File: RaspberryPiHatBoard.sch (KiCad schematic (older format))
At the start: 49 parts

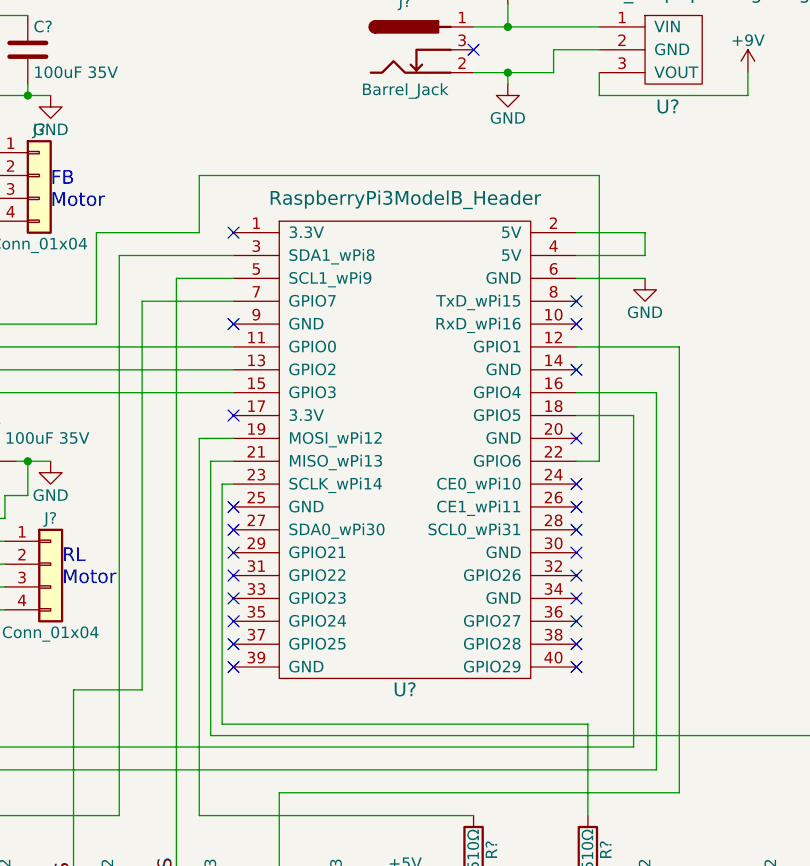
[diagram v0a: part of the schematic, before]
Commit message: Converted to pigpio
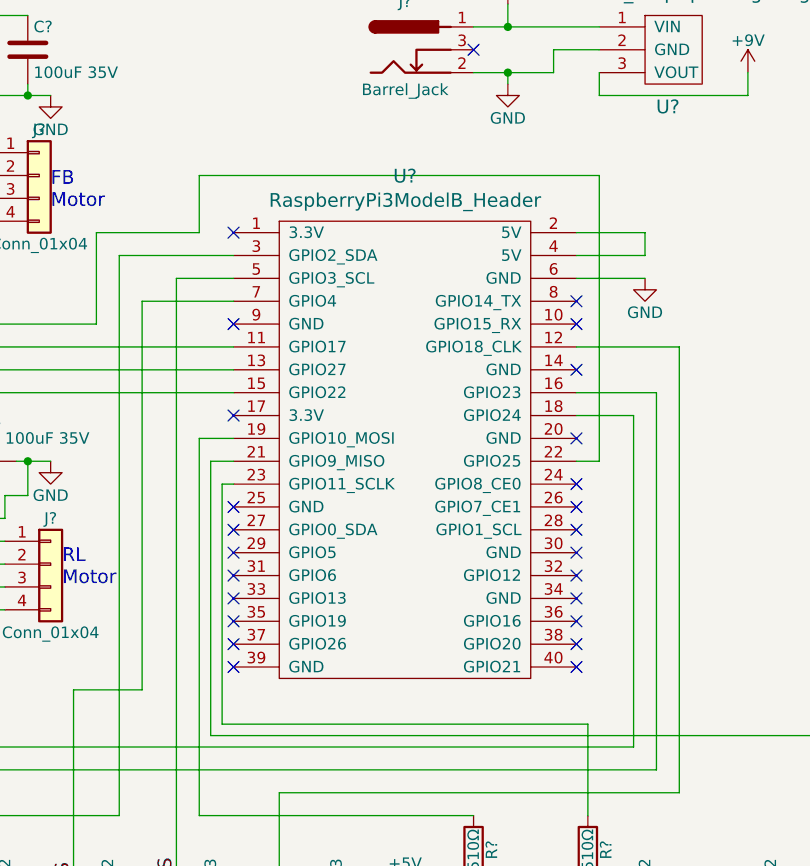
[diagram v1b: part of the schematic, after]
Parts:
- removed U?: RaspberryPi3ModelB_Header, symbol RaspberryPiHatBoard-rescue:RaspberryPi3ModelB_Header-LibraryRaspberryPiHatBoard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
- added U?: RaspberryPi3ModelB_Header, symbol LibraryRaspberryPiHatBoard:RaspberryPi3ModelB_Header
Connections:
- net FB_S: now also U?.7 (GPIO4)
- net GND: now also U?.6 (GND)
- net RL_S: now also U?.3 (GPIO2_SDA)
- net UD_S: now also U?.5 (GPIO3_SCL)
- net at U?.6 (~SLEEP): now also U?.11 (GPIO17)
- net at J?.1 (Pin_1): now also U?.12 (GPIO18_CLK)
- net at U?.8 (DIR): now also U?.13 (GPIO27)
- net at U?.6 (~SLEEP): now also U?.15 (GPIO22)
- net at U?.7 (Step): now also U?.16 (GPIO23)
- net at U?.8 (DIR): now also U?.18 (GPIO24)
- net at R?.1: now also U?.19 (GPIO10_MOSI)
- net at J?.1 (Pin_1): now also U?.21 (GPIO9_MISO)
- net at U?.7 (Step): now also U?.22 (GPIO25)
- net at R?.1: now also U?.23 (GPIO11_SCLK)
- new net: U?.2 (5V), U?.4 (5V)
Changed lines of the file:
@@
 $EndDescr
-$Comp
-L RaspberryPiHatBoard-rescue:RaspberryPi3ModelB_Header-LibraryRaspberryPiHatBoard-RaspberryPiHatBoard-rescue U?
-U 1 1 5AC0119C
-P 4750 3200
-F 0 "U?" H 4900 1550 60  0000 C CNN
-F 1 "RaspberryPi3ModelB_Header" H 4900 3700 60  0000 C CNN
-F 2 "" H 4750 3200 60  0001 C CNN
-F 3 "" H 4750 3200 60  0001 C CNN
-	1    4750 3200
-	1    0    0    -1
-$EndComp
 $Comp
 L RaspberryPiHatBoard-rescue:DRV8834LowVoltageStepperMotorDriverCarrier-LibraryRaspberryPiHatBoard-RaspberryPiHatBoard-rescue U?
@@
 Wire Wire Line
 	9300 4350 9300 4650
+$Comp
+L LibraryRaspberryPiHatBoard:RaspberryPi3ModelB_Header U?
+U 1 1 646EC029
+P 4750 3200
+F 0 "U?" H 4900 3797 60  0000 C CNN
+F 1 "RaspberryPi3ModelB_Header" H 4900 3691 60  0000 C CNN
+F 2 "" H 4750 3200 60  0001 C CNN
+F 3 "" H 4750 3200 60  0001 C CNN
+	1    4750 3200
+	1    0    0    -1
+$EndComp
 $EndSCHEMATC
